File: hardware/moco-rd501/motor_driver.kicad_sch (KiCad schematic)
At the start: 71 parts, among them Q1 CSD18540Q5B, Q2 CSD18540Q5B, Q3 CSD18540Q5B, Q4 CSD18540Q5B, Q5 CSD18540Q5B, Q6 CSD18540Q5B, U2 DRV8301

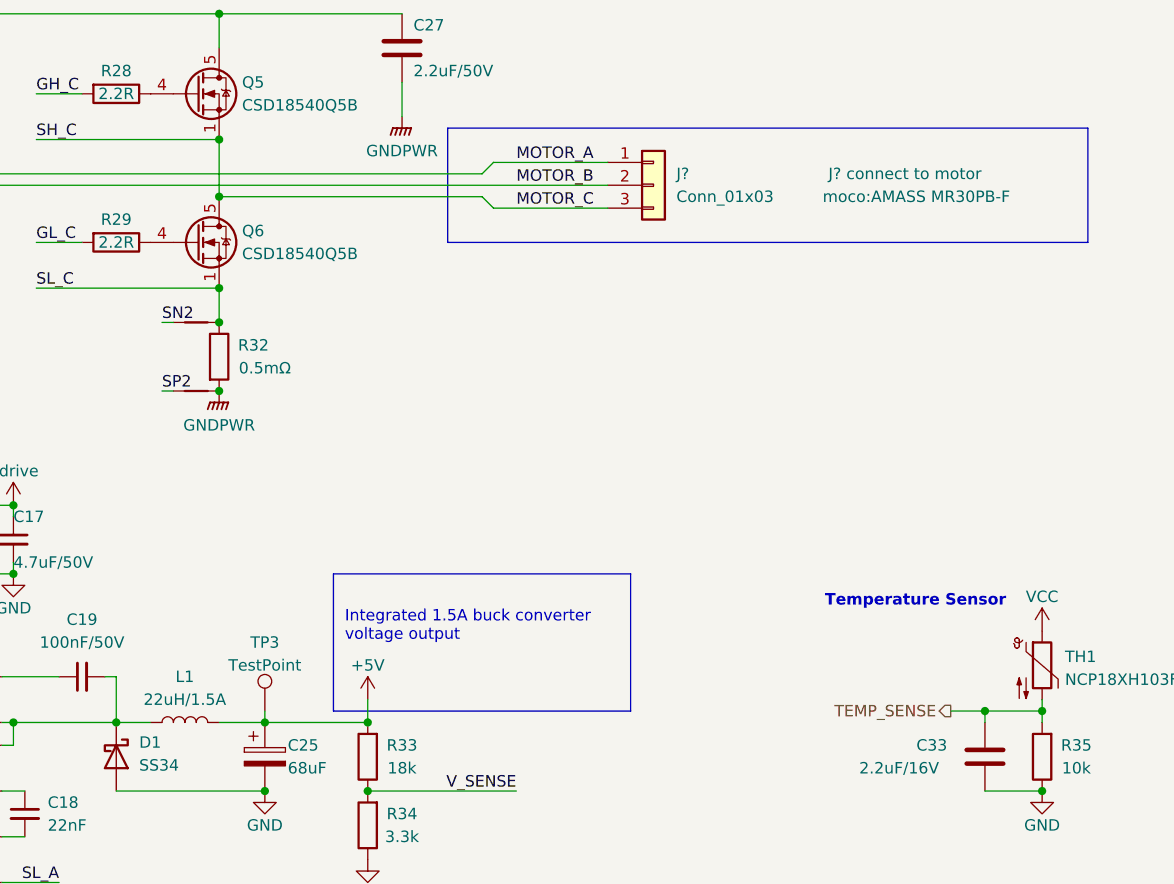
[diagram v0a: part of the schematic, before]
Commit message: Rename "moco-s" to "moco-rd501"
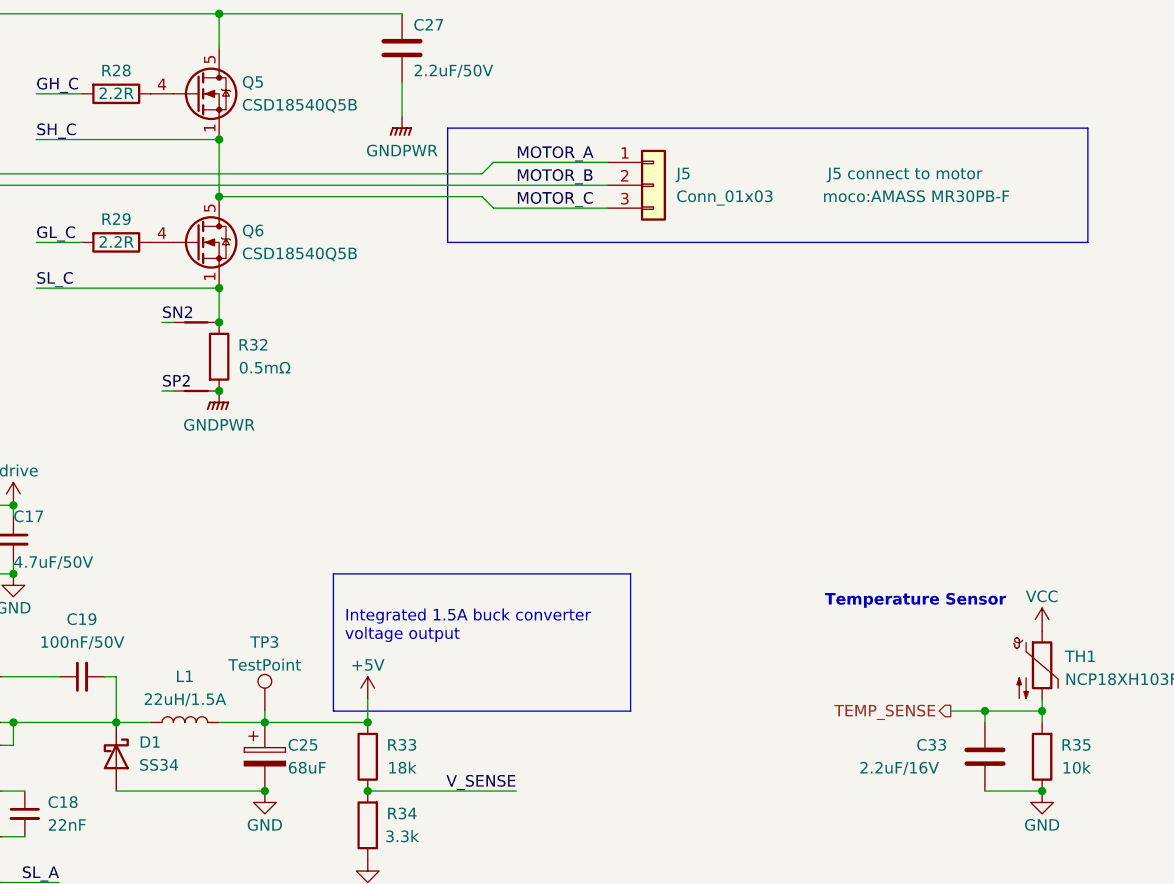
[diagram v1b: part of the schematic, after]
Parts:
- gave numbers to parts that had none: 1
